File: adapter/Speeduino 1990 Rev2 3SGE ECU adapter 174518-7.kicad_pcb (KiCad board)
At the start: 2 copper layers, 137.2 x 45.6 mm, 17 parts, among them J1 Conn_02x20_Odd_Even, J2 Screw_Terminal_01x02, P1 CONN_3, P10 CONN_8, P11 CONN_8, P12 CONN_8, P13 CONN_8, P2 CONN_3, P3 Conn_01x04_Male, P4 CONN_1, P5 CONN_1, P6 Conn_01x04_Male, P7 174518-7, P8 CONN_8, P9 CONN_8

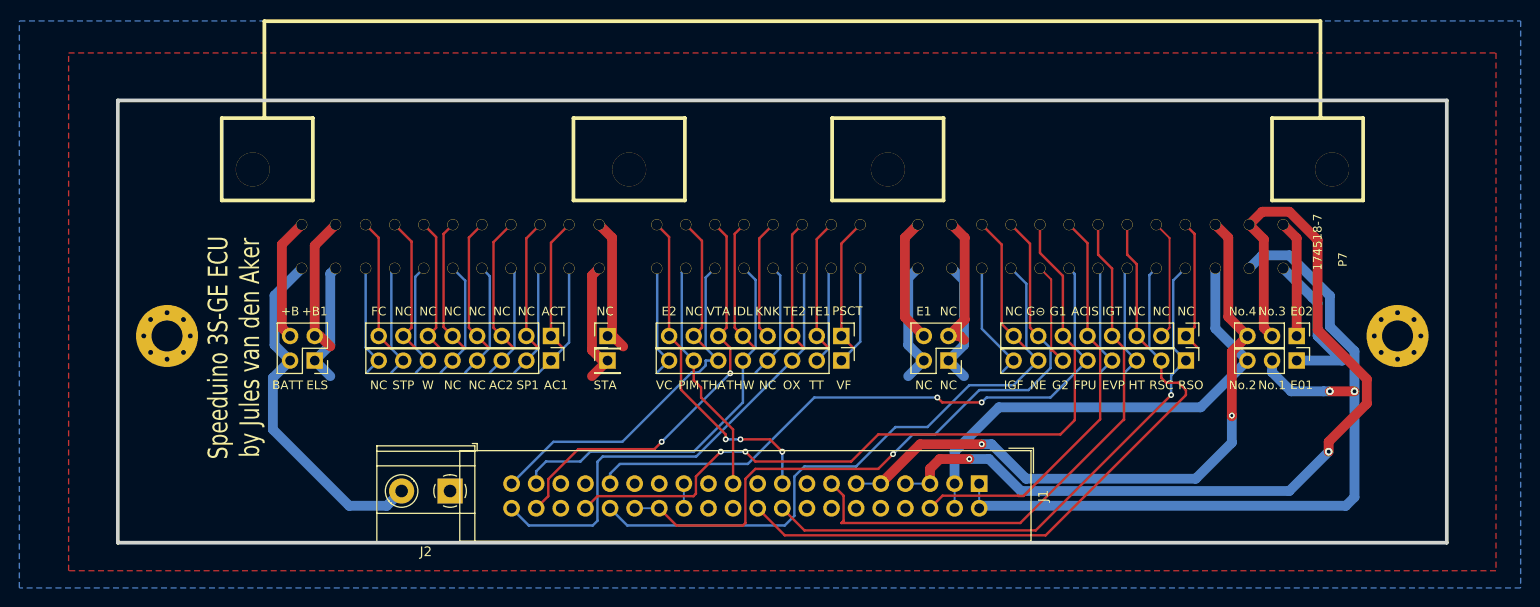
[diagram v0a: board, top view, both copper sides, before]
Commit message: Finished adapter board, slight changes to ECU
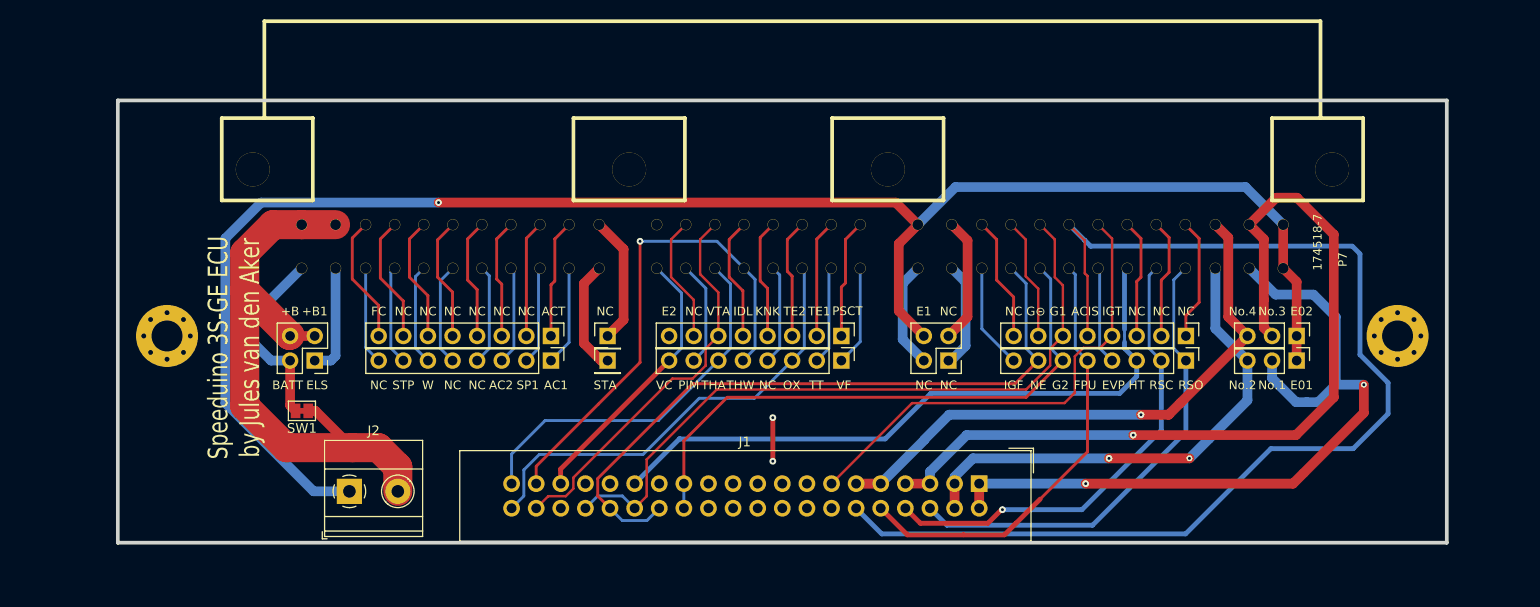
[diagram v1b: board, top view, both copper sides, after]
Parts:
- added SW1: SW_SPST, Jumper:SolderJumper-2_P1.3mm_Bridged_Pad1.0x1.5mm, F.Cu at (69.8, 72.5)
- moved J2 10.4 mm to (74.7, 80.8), turned to 0 degrees
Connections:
- net IGT renamed IGN-1-OUT
- net TPS_Sensor renamed TPS-IN
- J1 pad 12: BOOST-OUT -> ACIS-OUT
- J1 pad 14: IGN-2-OUT -> unconnected-(J1-Pad14)
- J1 pad 15: IGN-4-OUT -> unconnected-(J1-Pad15)
- J1 pad 16: IGN-3-OUT -> unconnected-(J1-Pad16)
- J1 pad 17: GNDREF -> GND
- J1 pad 18: RSO -> unconnected-(J1-Pad18)
- J1 pad 20: RSC -> unconnected-(J1-Pad20)
- J1 pad 21: MAP-EXT -> unconnected-(J1-Pad21)
- J1 pad 22: STEP-B1 -> unconnected-(J1-Pad22)
- J1 pad 24: STEP-B2 -> unconnected-(J1-Pad24)
- J1 pad 25: VDDA -> CAM2-IN
- J1 pad 26: VDDA -> CAM2-IN
- J1 pad 27: PROTO-1 -> unconnected-(J1-Pad27)
- J1 pad 28: G- -> CRANK-IN
- J1 pad 29: PROTO-2 -> HT-OUT
- J1 pad 30: G- -> CAM1-IN
- J1 pad 31: PROTO-3 -> unconnected-(J1-Pad31)
- J1 pad 32: NE -> CRANK-IN
- J1 pad 33: PROTO-4 -> unconnected-(J1-Pad33)
- J1 pad 34: G1 -> CAM1-IN
- J1 pad 35: PROTO-5 -> VDDA
- J1 pad 37: CLT_Sensor -> CLT-IN
- J1 pad 39: IAT_Sensor -> IAT-IN
- J1 pad 40: O2_Sensor -> O2-IN
- J1 pad 6: ACIS -> HC-2-OUT
- J1 pad 8: x -> IDLE-OUT
- J2 pad 1: GND -> GND1
- J2 pad 2: Net-(P7-Pad14) -> Net-(J2-Pad2)
- P1 pad 1: GND -> GND1
- P10 pad 2: unconnected-(P10-Pad2) -> Net-(P10-Pad2)
- P10 pad 3: Net-(P10-Pad3) -> O2-IN
- P10 pad 4: unconnected-(P10-Pad4) -> Net-(P10-Pad4)
- P10 pad 5: Net-(P10-Pad5) -> CLT-IN
- P10 pad 6: Net-(P10-Pad6) -> IAT-IN
- P10 pad 7: MAP-EXT -> Net-(P10-Pad7)
- P10 pad 8: Net-(P10-Pad8) -> VDDA
- P11 pad 1: unconnected-(P11-Pad1) -> Net-(P11-Pad1)
- P11 pad 5: IDLE-OUT -> Net-(P11-Pad5)
- P11 pad 7: unconnected-(P11-Pad7) -> Net-(P11-Pad7)
- P11 pad 8: GNDREF -> GND
- P12 pad 3: unconnected-(P12-Pad3) -> Net-(P12-Pad3)
- P12 pad 4: unconnected-(P12-Pad4) -> Net-(P12-Pad4)
- P12 pad 5: unconnected-(P12-Pad5) -> Net-(P12-Pad5)
- P12 pad 8: unconnected-(P12-Pad8) -> Net-(P12-Pad8)
- P13 pad 2: unconnected-(P13-Pad2) -> Net-(P13-Pad2)
- P13 pad 3: unconnected-(P13-Pad3) -> Net-(P13-Pad3)
- P13 pad 4: unconnected-(P13-Pad4) -> Net-(P13-Pad4)
- P13 pad 5: unconnected-(P13-Pad5) -> Net-(P13-Pad5)
- P13 pad 6: unconnected-(P13-Pad6) -> Net-(P13-Pad6)
- P13 pad 7: unconnected-(P13-Pad7) -> Net-(P13-Pad7)
- P2 pad 1: GND -> GND1
- P3 pad 1: unconnected-(P3-Pad1) -> Net-(P3-Pad1)
- P3 pad 2: unconnected-(P3-Pad2) -> Net-(P3-Pad2)
- P3 pad 3: unconnected-(P3-Pad3) -> Net-(P3-Pad3)
- P3 pad 4: GND -> GND1
- P5 pad 1: unconnected-(P5-Pad1) -> Net-(P5-Pad1)
- P6 pad 2: Net-(P7-Pad14) -> Net-(P6-Pad2)
- P6 pad 3: Net-(P7-Pad15) -> Net-(J2-Pad2)
- P6 pad 4: Net-(P7-Pad16) -> Net-(J2-Pad2)
- P7 pad 1: GND -> GND1
- P7 pad 10: GND -> GND1
- P7 pad 12: unconnected-(P5-Pad1) -> Net-(P5-Pad1)
- P7 pad 14: Net-(P7-Pad14) -> Net-(P6-Pad2)
- P7 pad 15: Net-(P7-Pad15) -> Net-(J2-Pad2)
- P7 pad 16: Net-(P7-Pad16) -> Net-(J2-Pad2)
- P7 pad 17: RSO -> HC-2-OUT
- P7 pad 18: RSC -> IDLE-OUT
- P7 pad 19: Net-(P7-Pad19) -> HT-OUT
- P7 pad 21: PROTO-3 -> HC-1-OUT
- P7 pad 22: G2 -> CAM2-IN
- P7 pad 23: NE -> CRANK-IN
- P7 pad 25: unconnected-(P7-Pad25) -> Net-(P7-Pad25)
- P7 pad 26: unconnected-(P7-Pad26) -> Net-(P7-Pad26)
- P7 pad 27: unconnected-(P7-Pad27) -> Net-(P7-Pad27)
- P7 pad 29: ACIS -> ACIS-OUT
- P7 pad 30: G1 -> CAM1-IN
- P7 pad 31: G- -> GND
- P7 pad 32: unconnected-(P7-Pad32) -> Net-(P7-Pad32)
- P7 pad 34: unconnected-(P10-Pad2) -> Net-(P10-Pad2)
- P7 pad 35: Net-(P10-Pad3) -> O2-IN
- P7 pad 36: unconnected-(P10-Pad4) -> Net-(P10-Pad4)
- P7 pad 37: Net-(P10-Pad5) -> CLT-IN
- P7 pad 38: Net-(P10-Pad6) -> IAT-IN
- P7 pad 39: MAP-EXT -> Net-(P10-Pad7)
- P7 pad 4: GND -> GND1
- P7 pad 40: Net-(P10-Pad8) -> VDDA
- P7 pad 41: unconnected-(P11-Pad1) -> Net-(P11-Pad1)
- P7 pad 45: unconnected-(P11-Pad5) -> Net-(P11-Pad5)
- P7 pad 47: unconnected-(P11-Pad7) -> Net-(P11-Pad7)
- P7 pad 48: GNDREF -> GND
- P7 pad 51: unconnected-(P12-Pad3) -> Net-(P12-Pad3)
- P7 pad 52: unconnected-(P12-Pad4) -> Net-(P12-Pad4)
- P7 pad 53: unconnected-(P12-Pad5) -> Net-(P12-Pad5)
- P7 pad 56: unconnected-(P12-Pad8) -> Net-(P12-Pad8)
- P7 pad 58: unconnected-(P13-Pad2) -> Net-(P13-Pad2)
- P7 pad 59: unconnected-(P13-Pad3) -> Net-(P13-Pad3)
- P7 pad 60: unconnected-(P13-Pad4) -> Net-(P13-Pad4)
- P7 pad 61: unconnected-(P13-Pad5) -> Net-(P13-Pad5)
- P7 pad 62: unconnected-(P13-Pad6) -> Net-(P13-Pad6)
- P7 pad 63: unconnected-(P13-Pad7) -> Net-(P13-Pad7)
- P7 pad 7: unconnected-(P3-Pad1) -> Net-(P3-Pad1)
- P7 pad 8: unconnected-(P3-Pad2) -> Net-(P3-Pad2)
- P7 pad 9: unconnected-(P3-Pad3) -> Net-(P3-Pad3)
- P8 pad 1: RSO -> HC-2-OUT
- P8 pad 2: RSC -> IDLE-OUT
- P8 pad 3: Net-(P7-Pad19) -> HT-OUT
- P8 pad 5: PROTO-3 -> HC-1-OUT
- P8 pad 6: G2 -> CAM2-IN
- P8 pad 7: NE -> CRANK-IN
- P9 pad 1: unconnected-(P7-Pad25) -> Net-(P7-Pad25)
- P9 pad 2: unconnected-(P7-Pad26) -> Net-(P7-Pad26)
- P9 pad 3: unconnected-(P7-Pad27) -> Net-(P7-Pad27)
- P9 pad 5: ACIS -> ACIS-OUT
- P9 pad 6: G1 -> CAM1-IN
- P9 pad 7: G- -> GND
- P9 pad 8: unconnected-(P7-Pad32) -> Net-(P7-Pad32)
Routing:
- net GND1: track 0.00 -> 176.4 mm, vias 0 -> 1
- net ACIS-OUT: track 0.00 -> 122.4 mm
- net G1: track 77.8 -> 0.00 mm, vias 2 -> 0
- net CAM1-IN: track 0.00 -> 73.4 mm
- net CRANK-IN: track 0.00 -> 70.9 mm
- net G-: track 69.5 -> 0.00 mm, vias 1 -> 0
- net HT-OUT: track 0.00 -> 68.2 mm
- net RSC: track 67.0 -> 0.00 mm
- net PROTO-3: track 65.9 -> 0.00 mm, vias 2 -> 0
- net NE: track 65.1 -> 0.00 mm
- net Net-(J2-Pad2): track 0.00 -> 62.6 mm
- net RSO: track 61.6 -> 0.00 mm, vias 1 -> 0
- net CAM2-IN: track 0.00 -> 60.0 mm
- net CLT-IN: track 0.00 -> 51.9 mm, vias 0 -> 1
- net Net-(P10-Pad3): track 50.4 -> 0.00 mm
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- removed copper zone on F.Cu, net GND
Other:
- board text added: "Fontys Engineering Eindhoven EXPO Group 13 Fall 2022"
